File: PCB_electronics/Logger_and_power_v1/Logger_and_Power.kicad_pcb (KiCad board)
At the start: 2 copper layers, 106.5 x 127 mm, 46 parts, among them IC1 ATMEGA328-P, P1 SOLAR_PANEL, P10 CONN_01X08, P11 CONN_01X08, P12 CONN_01X03, P13 CONN_01X02, P14 CONN_01X02, P15 CONN_01X02, P16 Iridium_header_high, P17 Iridium_header_low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

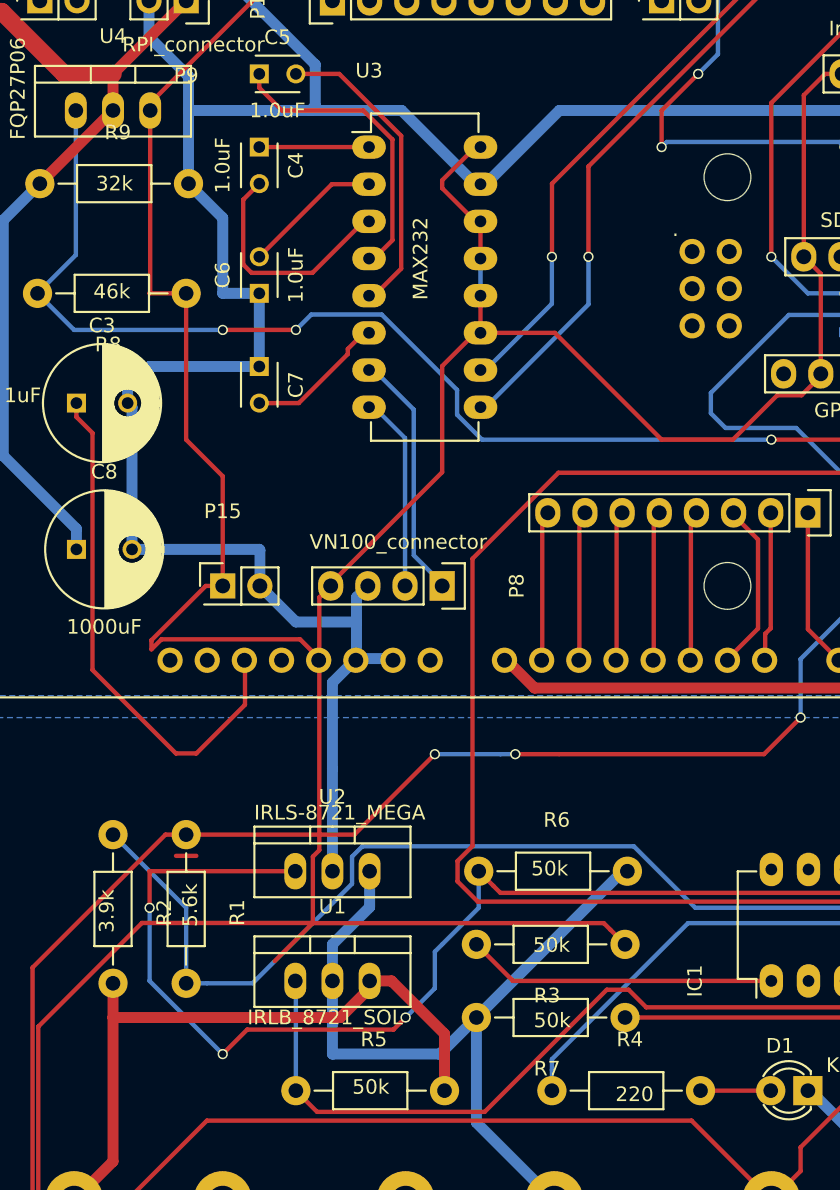
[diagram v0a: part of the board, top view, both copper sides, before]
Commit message: now the v3.5 of the PCB: v3, integrated Pololu, with correct names on the PCB
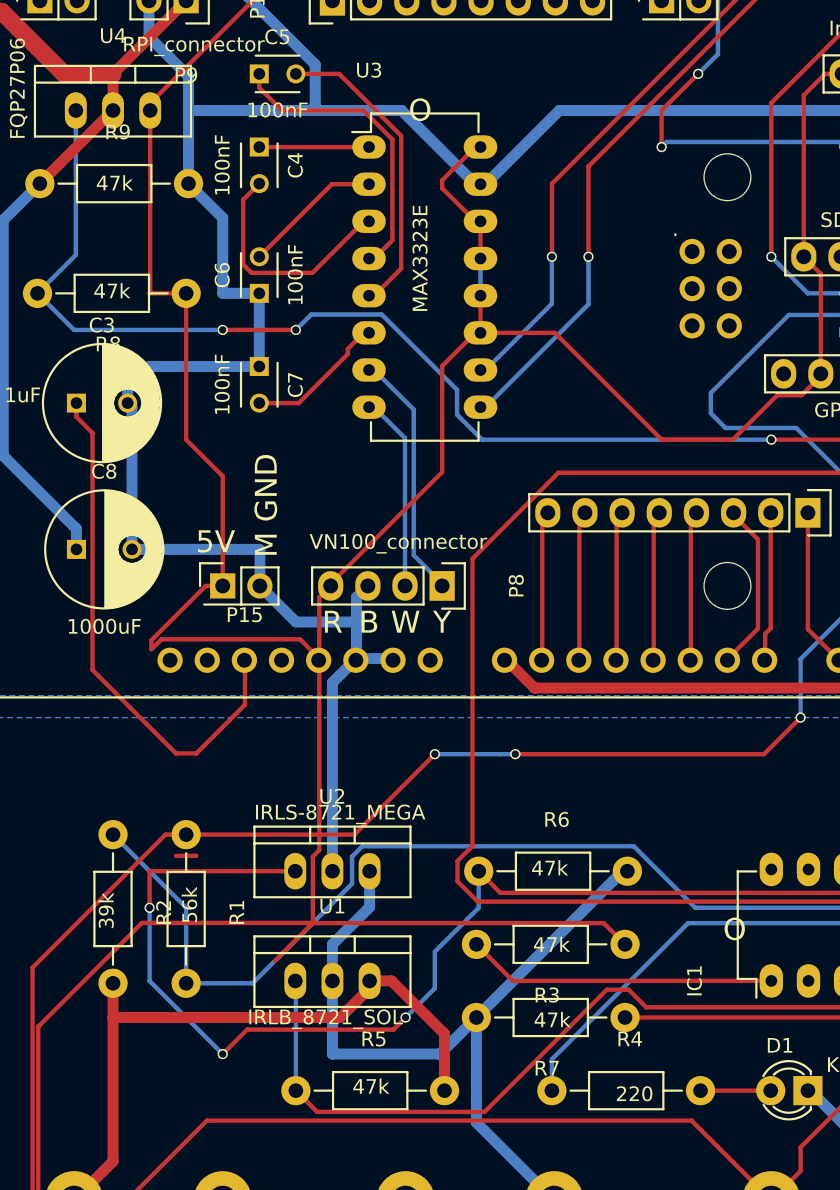
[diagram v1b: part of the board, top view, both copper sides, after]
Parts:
- C4, C5, C6, C7: value 1.0uF -> 100nF
- R1: value 5.6k -> 56k
- R2: value 3.9k -> 39k
- R3, R5, R6, R7: value 50k -> 47k
- R8: value 46k -> 47k
- R9: value 32k -> 47k
- U3: value MAX232 -> MAX3323E
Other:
- board text added: "5V"
- board text added: "B"
- board text added: "M GND"
- board text added: "O"
- board text added: "Power and Logger with headers v3.5 Jean Rabault, UiO 07-2019"
- board text added: "R"
- board text added: "W"
- board text added: "Y"
- board text removed: "Power and Logger with headers v3.0 Jean Rabault, UiO 07-2019"
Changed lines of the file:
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@@
     (area 141.734999 30.5 271.500001 163.000001)
     (thickness 1.6)
-    (drawings 20)
+    (drawings 28)
     (tracks 668)
     (zones 0)
@@
   (page A4)
   (layers
-    (0 F.Cu signal)
+    (0 F.Cu signal hide)
     (31 B.Cu signal hide)
     (32 B.Adhes user hide)
@@
       (effects (font (size 1 1) (thickness 0.15)))
     )
-    (fp_text value 1.0uF (at 1.25 2.5 270) (layer F.SilkS)
+    (fp_text value 100nF (at 1.25 2.5 270) (layer F.SilkS)
       (effects (font (size 1 1) (thickness 0.15)))
     )
@@
       (effects (font (size 1 1) (thickness 0.15)))
     )
-    (fp_text value 1.0uF (at 1.25 2.5) (layer F.SilkS)
+    (fp_text value 100nF (at 1.25 2.5) (layer F.SilkS)
       (effects (font (size 1 1) (thickness 0.15)))
     )
@@
       (effects (font (size 1 1) (thickness 0.15)))
     )
-    (fp_text value 1.0uF (at 1.25 2.5 90) (layer F.SilkS)
+    (fp_text value 100nF (at 1.25 2.5 90) (layer F.SilkS)
       (effects (font (size 1 1) (thickness 0.15)))
     )
@@
       (effects (font (size 1 1) (thickness 0.15)))
     )
-    (fp_text value 1.0uF (at 1.25 2.5 270) (layer F.Fab)
+    (fp_text value 100nF (at 1.25 2.5 270) (layer F.SilkS)
       (effects (font (size 1 1) (thickness 0.15)))
     )
@@
     (descr "Through hole pin header")
     (tags "pin header")
-    (fp_text reference P15 (at 0 -5.1) (layer F.SilkS)
+    (fp_text reference P15 (at 1.5 2) (layer F.SilkS)
       (effects (font (size 1 1) (thickness 0.15)))
     )
@@
       (effects (font (size 1 1) (thickness 0.15)))
     )
-    (fp_text value 5.6k (at 4.825 -0.275 270) (layer F.SilkS)
+    (fp_text value 56k (at 4.825 -0.275 270) (layer F.SilkS)
       (effects (font (size 1 1) (thickness 0.15)))
     )
@@
       (effects (font (size 1 1) (thickness 0.15)))
     )
-    (fp_text value 3.9k (at 5.225 0.425 270) (layer F.SilkS)
+    (fp_text value 39k (at 5.225 0.425 270) (layer F.SilkS)
       (effects (font (size 1 1) (thickness 0.15)))
     )
@@
       (effects (font (size 1 1) (thickness 0.15)))
     )
-    (fp_text value 50k (at 5.15 5.175 180) (layer F.SilkS)
+    (fp_text value 47k (at 5.15 5.175 180) (layer F.SilkS)
       (effects (font (size 1 1) (thickness 0.15)))
     )
@@
       (effects (font (size 1 1) (thickness 0.15)))
     )
-    (fp_text value 50k (at 5.125 -0.25) (layer F.SilkS)
+    (fp_text value 47k (at 5.125 -0.25) (layer F.SilkS)
       (effects (font (size 1 1) (thickness 0.15)))
     )
@@
       (effects (font (size 1 1) (thickness 0.15)))
     )
-    (fp_text value 50k (at 4.975 5.05) (layer F.SilkS)
+    (fp_text value 47k (at 4.975 5.05) (layer F.SilkS)
       (effects (font (size 1 1) (thickness 0.15)))
     )
@@
       (effects (font (size 1 1) (thickness 0.15)))
     )
-    (fp_text value 50k (at 4.975 -0.2 180) (layer F.SilkS)
+    (fp_text value 47k (at 4.975 -0.2 180) (layer F.SilkS)
       (effects (font (size 1 1) (thickness 0.15)))
     )
@@
       (effects (font (size 1 1) (thickness 0.15)))
     )
-    (fp_text value 46k (at 5.075 0.125 180) (layer F.SilkS)
+    (fp_text value 47k (at 5.075 0.125 180) (layer F.SilkS)
       (effects (font (size 1 1) (thickness 0.15)))
     )
@@
       (effects (font (size 1 1) (thickness 0.15)))
     )
-    (fp_text value 32k (at 5.1 0) (layer F.SilkS)
+    (fp_text value 47k (at 5.1 0) (layer F.SilkS)
       (effects (font (size 1 1) (thickness 0.15)))
     )
@@
       (effects (font (size 1 1) (thickness 0.15)))
     )
-    (fp_text value MAX232 (at 3.525 7.625 90) (layer F.SilkS)
+    (fp_text value MAX3323E (at 3.525 7.625 90) (layer F.SilkS)
       (effects (font (size 1 1) (thickness 0.15)))
     )
@@
     )
   )
+  (gr_text O (at 215 121) (layer F.SilkS)
+    (effects (font (size 1.5 1.5) (thickness 0.3)))
+  )
+  (gr_text O (at 193.5 65) (layer F.SilkS)
+    (effects (font (size 1.5 1.5) (thickness 0.3)))
+  )
+  (gr_text Y (at 195 100) (layer F.SilkS)
+    (effects (font (size 1.5 1.5) (thickness 0.3)))
+  )
+  (gr_text W (at 192.5 100) (layer F.SilkS)
+    (effects (font (size 1.5 1.5) (thickness 0.3)))
+  )
+  (gr_text B (at 190 100) (layer F.SilkS)
+    (effects (font (size 1.5 1.5) (thickness 0.3)))
+  )
+  (gr_text R (at 187.5 100) (layer F.SilkS)
+    (effects (font (size 1.5 1.5) (thickness 0.3)))
+  )
+  (gr_text "M GND" (at 183 92 90) (layer F.SilkS)
+    (effects (font (size 1.5 1.5) (thickness 0.3)))
+  )
+  (gr_text 5V (at 179.5 94.5) (layer F.SilkS)
+    (effects (font (size 1.5 1.5) (thickness 0.3)))
+  )
   (gr_text "GND pololu" (at 223 146) (layer F.SilkS)
     (effects (font (size 1.5 1.5) (thickness 0.3)))
@@
   (gr_line (start 185.5 32) (end 185.5 42) (layer Edge.Cuts) (width 0.15))
   (gr_line (start 188.5 32) (end 185.5 32) (layer Edge.Cuts) (width 0.15))
-  (gr_text "Power and Logger with headers v3.0\nJean Rabault, UiO\n07-2019" (at 234.875 111.875) (layer B.SilkS)
+  (gr_text "Power and Logger with headers v3.5\nJean Rabault, UiO\n07-2019" (at 234.875 111.875) (layer B.SilkS)
     (effects (font (size 1.5 1.5) (thickness 0.3)) (justify mirror))
   )

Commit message: v3.6 with a bit more on the PCB silk mask
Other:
- board text added: "+"
- board text added: "-"
- board text added: "Power and Logger with headers v3.6 Jean Rabault, UiO 10-2019"
- board text removed: "Power and Logger with headers v3.5 Jean Rabault, UiO 07-2019"
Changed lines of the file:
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@@
     (area 141.734999 30.5 271.500001 163.000001)
     (thickness 1.6)
-    (drawings 28)
+    (drawings 36)
     (tracks 668)
     (zones 0)
@@
     )
   )
+  (gr_text + (at 255 137.5) (layer F.SilkS)
+    (effects (font (size 1.5 1.5) (thickness 0.3)))
+  )
+  (gr_text - (at 242 136) (layer F.SilkS)
+    (effects (font (size 1.5 1.5) (thickness 0.3)))
+  )
+  (gr_text - (at 227.5 136) (layer F.SilkS)
+    (effects (font (size 1.5 1.5) (thickness 0.3)))
+  )
+  (gr_text + (at 217.5 136) (layer F.SilkS)
+    (effects (font (size 1.5 1.5) (thickness 0.3)))
+  )
+  (gr_text - (at 202.5 136) (layer F.SilkS)
+    (effects (font (size 1.5 1.5) (thickness 0.3)))
+  )
+  (gr_text + (at 192.5 136) (layer F.SilkS)
+    (effects (font (size 1.5 1.5) (thickness 0.3)))
+  )
+  (gr_text + (at 180 136) (layer F.SilkS)
+    (effects (font (size 1.5 1.5) (thickness 0.3)))
+  )
+  (gr_text - (at 170 136) (layer F.SilkS)
+    (effects (font (size 1.5 1.5) (thickness 0.3)))
+  )
   (gr_text O (at 215 121) (layer F.SilkS)
     (effects (font (size 1.5 1.5) (thickness 0.3)))
@@
   (gr_line (start 185.5 32) (end 185.5 42) (layer Edge.Cuts) (width 0.15))
   (gr_line (start 188.5 32) (end 185.5 32) (layer Edge.Cuts) (width 0.15))
-  (gr_text "Power and Logger with headers v3.5\nJean Rabault, UiO\n07-2019" (at 234.875 111.875) (layer B.SilkS)
+  (gr_text "Power and Logger with headers v3.6\nJean Rabault, UiO\n10-2019" (at 234.875 111.875) (layer B.SilkS)
     (effects (font (size 1.5 1.5) (thickness 0.3)) (justify mirror))
   )
